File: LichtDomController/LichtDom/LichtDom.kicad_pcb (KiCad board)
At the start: 2 copper layers, 46 parts, among them J101 Conn_01x02_Male, J102 Raspberry_Pi_2_3, J103 Stecker der Lichtdomplatten, J104 Stecker des Zweifarb-Ringlich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, J105 0,96" OLED, U1 TPS5430DDA, U101 74HC595, U102 74HC595, U103 74HC595

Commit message: Controller grobe Abmessungen fertig
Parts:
- J102, J103, J104: moved to B.Cu
- moved D101 144.3 mm to (191.2, 154.8), turned to -90 degrees
- moved MK103 135.8 mm to (228.8, 159.8)
- moved MK101 134.6 mm to (182.8, 159.8)
- moved J105 118.9 mm to (133.2, 21.5)
- moved MK105 118.9 mm to (121.8, 22.0)
- moved MK106 118.9 mm to (152.2, 22.0)
- moved MK107 118.9 mm to (121.8, 50.5)
- moved MK108 118.9 mm to (152.2, 50.5)
- moved MK104 115.1 mm to (197.8, 148.8)
- moved J102 99.0 mm to (221.0, 84.0), turned to 180 degrees
- moved J101 78.7 mm to (197.8, 156.8)
- moved C104 67.0 mm to (204.9, 80.8)
- moved C102 55.6 mm to (204.9, 124.6)
- moved MK102 44.9 mm to (197.8, 78.8)
- moved U103 38.1 mm to (202.5, 133.0)
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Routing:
- net +24V: track 0.00 -> 96.7 mm
- net +3V3: track 0.00 -> 90.3 mm, vias 0 -> 8
- net /R1.1: track 0.00 -> 23.6 mm
- net /G1.4: track 0.00 -> 18.4 mm
- net /G1.3: track 0.00 -> 18.2 mm
- net /G1.1: track 0.00 -> 16.8 mm
- net /G1.2: track 0.00 -> 16.3 mm
- net /R5: track 0.00 -> 15.9 mm
- net /G8: track 0.00 -> 15.5 mm
- net /R1.3: track 0.00 -> 15.5 mm
- net /R1: track 0.00 -> 15.2 mm
- net /R1.4: track 0.00 -> 15.2 mm
- net /G4: track 0.00 -> 14.8 mm
- net /G7: track 0.00 -> 13.6 mm
- net /G3: track 0.00 -> 13.1 mm
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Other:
- board outline added: 56 x 90 mm
- rule solder_mask_min_width: 0.25 -> 0.15
- rule trace_min: 0.2 -> 0.16
- rule via_min_size: 0.4 -> 0.6

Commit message: Dom-Controller OLED gesetzt
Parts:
- moved MK106 115.2 mm to (213.5, 119.6), turned to -90 degrees
- moved MK105 113.7 mm to (213.5, 89.1), turned to -90 degrees
- moved J105 113.0 mm to (214.0, 100.5), turned to 0 degrees
- moved MK108 76.5 mm to (185.0, 119.6), turned to -90 degrees
- moved MK107 74.1 mm to (185.0, 89.1), turned to -90 degrees
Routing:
- net /I2C_SDA: track 0.00 -> 26.9 mm
- net /I2C_SCL: track 0.00 -> 20.9 mm
- net +3V3: track 90.3 -> 99.9 mm

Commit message: Layout quasi fertig - Texte ausgerichtet. Teilweise fehlen noch 3D-Daten!
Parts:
- moved TP102 193.8 mm to (230.5, 79.0)
- moved R3 186.4 mm to (216.0, 162.0), turned to 180 degrees
- moved C6 185.1 mm to (213.0, 138.2), turned to 180 degrees
- moved U1 184.8 mm to (216.0, 158.0)
- moved D1 184.0 mm to (223.5, 152.8), turned to -90 degrees
- moved C3 179.0 mm to (221.5, 159.0), turned to -90 degrees
- moved L1 177.4 mm to (215.5, 148.5), turned to -90 degrees
- moved R103 177.0 mm to (218.2, 79.8)
- moved TP103 176.0 mm to (224.0, 79.0)
- moved R101 173.7 mm to (213.6, 95.9)
- moved C1 172.9 mm to (206.0, 145.0), turned to -90 degrees
- moved C7 169.3 mm to (218.5, 141.2)
- moved R7 168.7 mm to (218.2, 77.8)
- moved R5 166.9 mm to (212.5, 162.0), turned to 180 degrees
- moved C2 164.4 mm to (206.0, 156.5), turned to -90 degrees
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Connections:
- C5 pad 1: Net-(C5-Pad1) -> +5V
- C6 pad 1: Net-(C5-Pad1) -> +5V
- C7 pad 1: Net-(C5-Pad1) -> +5V
- L1 pad 1: Net-(C5-Pad1) -> +5V
- R3 pad 1: Net-(C5-Pad1) -> +5V
- TP104 pad 1: Net-(C5-Pad1) -> +5V
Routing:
- net +5V: track 0.00 -> 192.5 mm, vias 0 -> 6
- net +24V: track 96.7 -> 201.1 mm, vias 0 -> 3
- net /SPI_CS: track 0.00 -> 67.8 mm, vias 0 -> 2
- net /WS2812B: track 0.00 -> 66.6 mm, vias 0 -> 2
- net /SPI_SCK: track 0.00 -> 63.2 mm, vias 0 -> 3
- net /SPI_MOSI: track 0.00 -> 38.7 mm
- net +3V3: track 99.9 -> 122.2 mm, vias 8 -> 9
- net /I2C_SDA: track 26.9 -> 49.1 mm, vias 0 -> 2
- net Net-(C4-Pad1): track 0.00 -> 21.3 mm
- net Net-(U102-Pad9): track 0.00 -> 20.4 mm
- net /I2C_SCL: track 20.9 -> 39.8 mm, vias 0 -> 1
- net Net-(C1-Pad2): track 0.00 -> 15.4 mm
- net Net-(U101-Pad9): track 0.00 -> 15.4 mm
- net Net-(R3-Pad2): track 0.00 -> 3.99 mm
- net Net-(C4-Pad2): track 0.00 -> 2.95 mm
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- added copper zone on F.Cu, net +3V3
- added copper zone on F.Cu, net +5V
- added copper zone on B.Cu, net GND
- added copper zone on F.Cu, net Net-(C4-Pad1)
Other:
- board text added: "+3,3V"
- board text added: "+5,0V"
- board text added: "24V 5V"

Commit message: 24V ordentlicher gemacht.
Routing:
- net +24V: track 201.1 -> 199.8 mm, vias 3 -> 1
- removed copper zone on F.Cu, net +5V
- removed copper zone on F.Cu, net Net-(C4-Pad1)

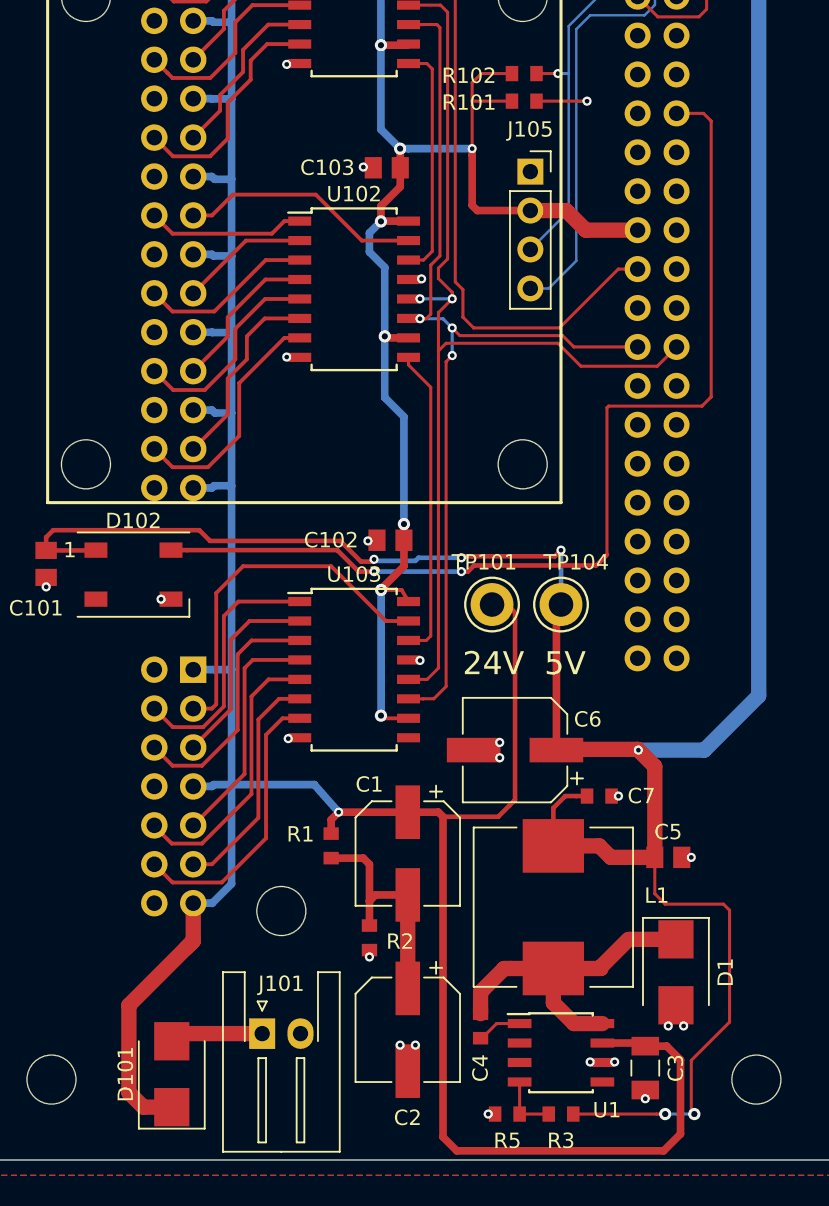
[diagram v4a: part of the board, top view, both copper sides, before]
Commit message: Lüfteranschluss hinzufügt.
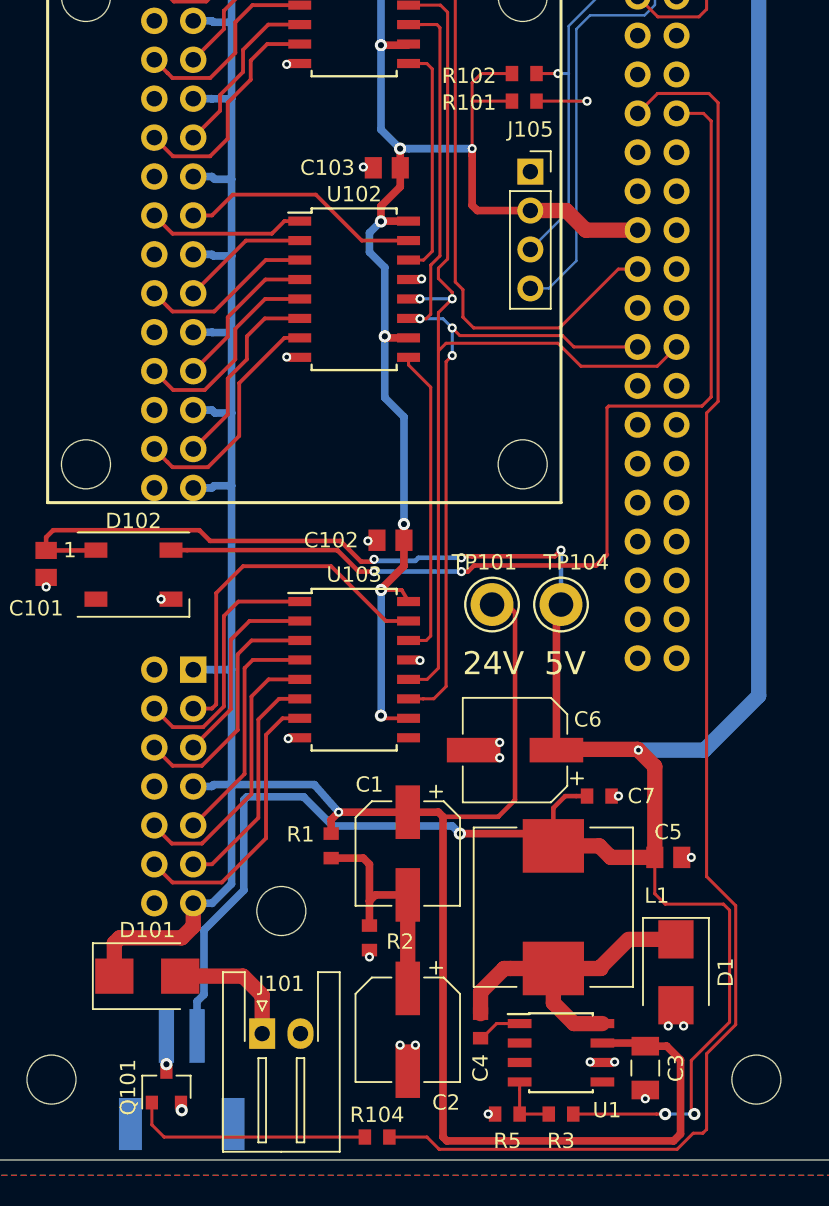
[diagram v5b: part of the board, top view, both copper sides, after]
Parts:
- added J106: Conn_01x02_Male, Connector_JST:JST_PH_S2B-PH-SM4-TB_1x02-1MP_P2.00mm_Horizontal, B.Cu at (191.2, 159.8)
- added Q101: BC817, Package_TO_SOT_SMD:SOT-23, F.Cu at (190.2, 160.2)
- added R104: 470, Resistor_SMD:R_0603_1608Metric, F.Cu at (204.0, 163.5)
- moved D101 6.60 mm to (189.0, 153.0), turned to 0 degrees
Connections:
- J102 pad 11: (no net) -> /Lüfter
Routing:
- net /Lüfter: track 0.00 -> 96.5 mm
- net +5V: track 192.8 -> 231.1 mm, vias 6 -> 7
- net Net-(Q101-Pad1): track 0.00 -> 15.7 mm
- net +24V: track 199.8 -> 190.5 mm
- net Net-(J106-Pad2): track 0.00 -> 2.35 mm, vias 0 -> 1
- net Net-(D101-Pad2): track 6.11 -> 8.37 mm
- net GND: vias 26 -> 27
